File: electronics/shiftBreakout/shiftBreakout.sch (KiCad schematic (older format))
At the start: 45 parts, among them J1 Screw_Terminal_01x05, J10 Sensor C, J11 Sensor D, J2 Screw_Terminal_01x06, J3 Motor A, J4 Screw_Terminal_01x05, J5 Motor B, J6 Motor C, J7 Motor D, J8 Sensor A, J9 Sensor B, U1 74HC595, U2 TPL7407L, U3 74HC244, U4 74HC165, U5 74HC595, U6 TPL7407L, U7 74HC595, U8 TPL7407L

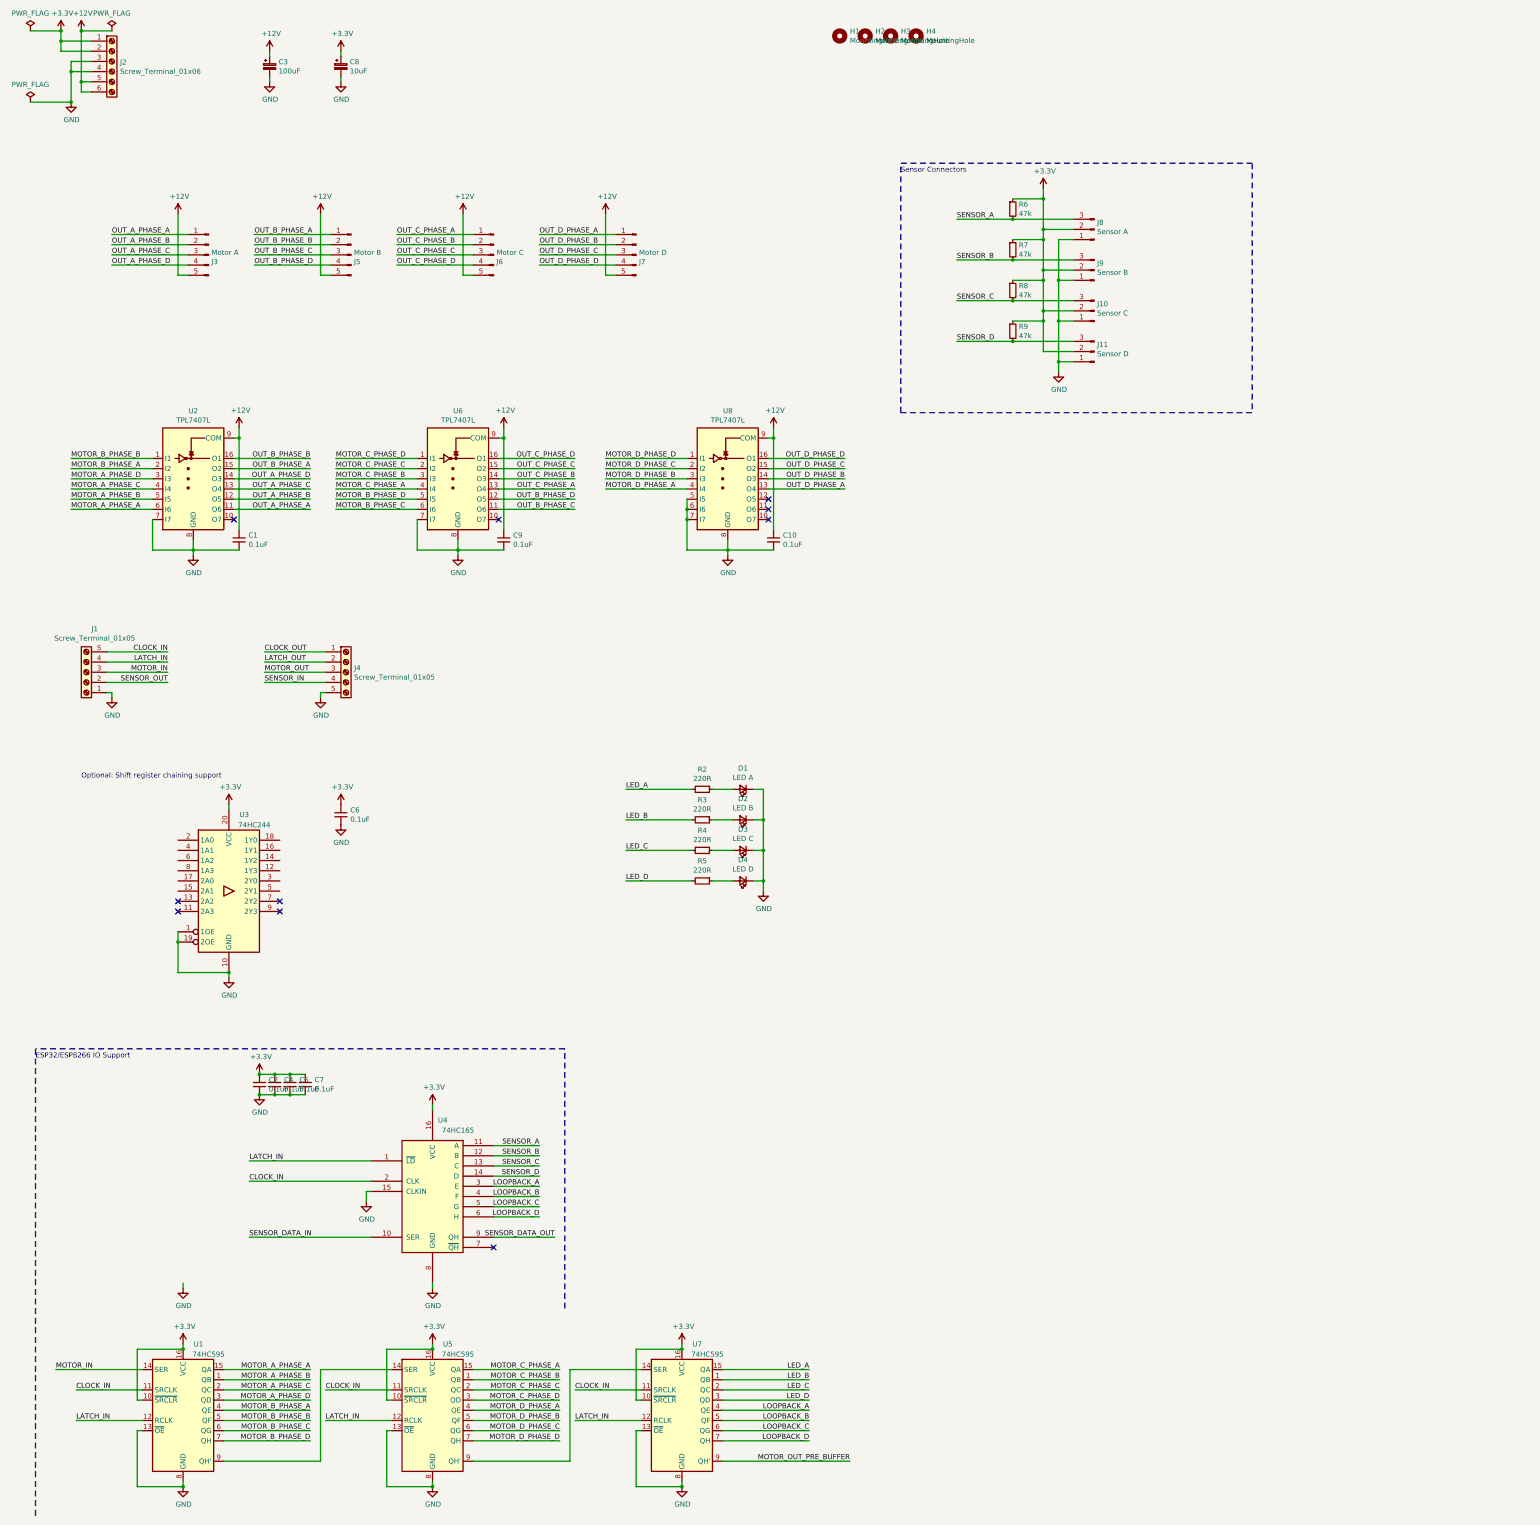
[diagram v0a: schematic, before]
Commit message: Shift breakout PCB progress
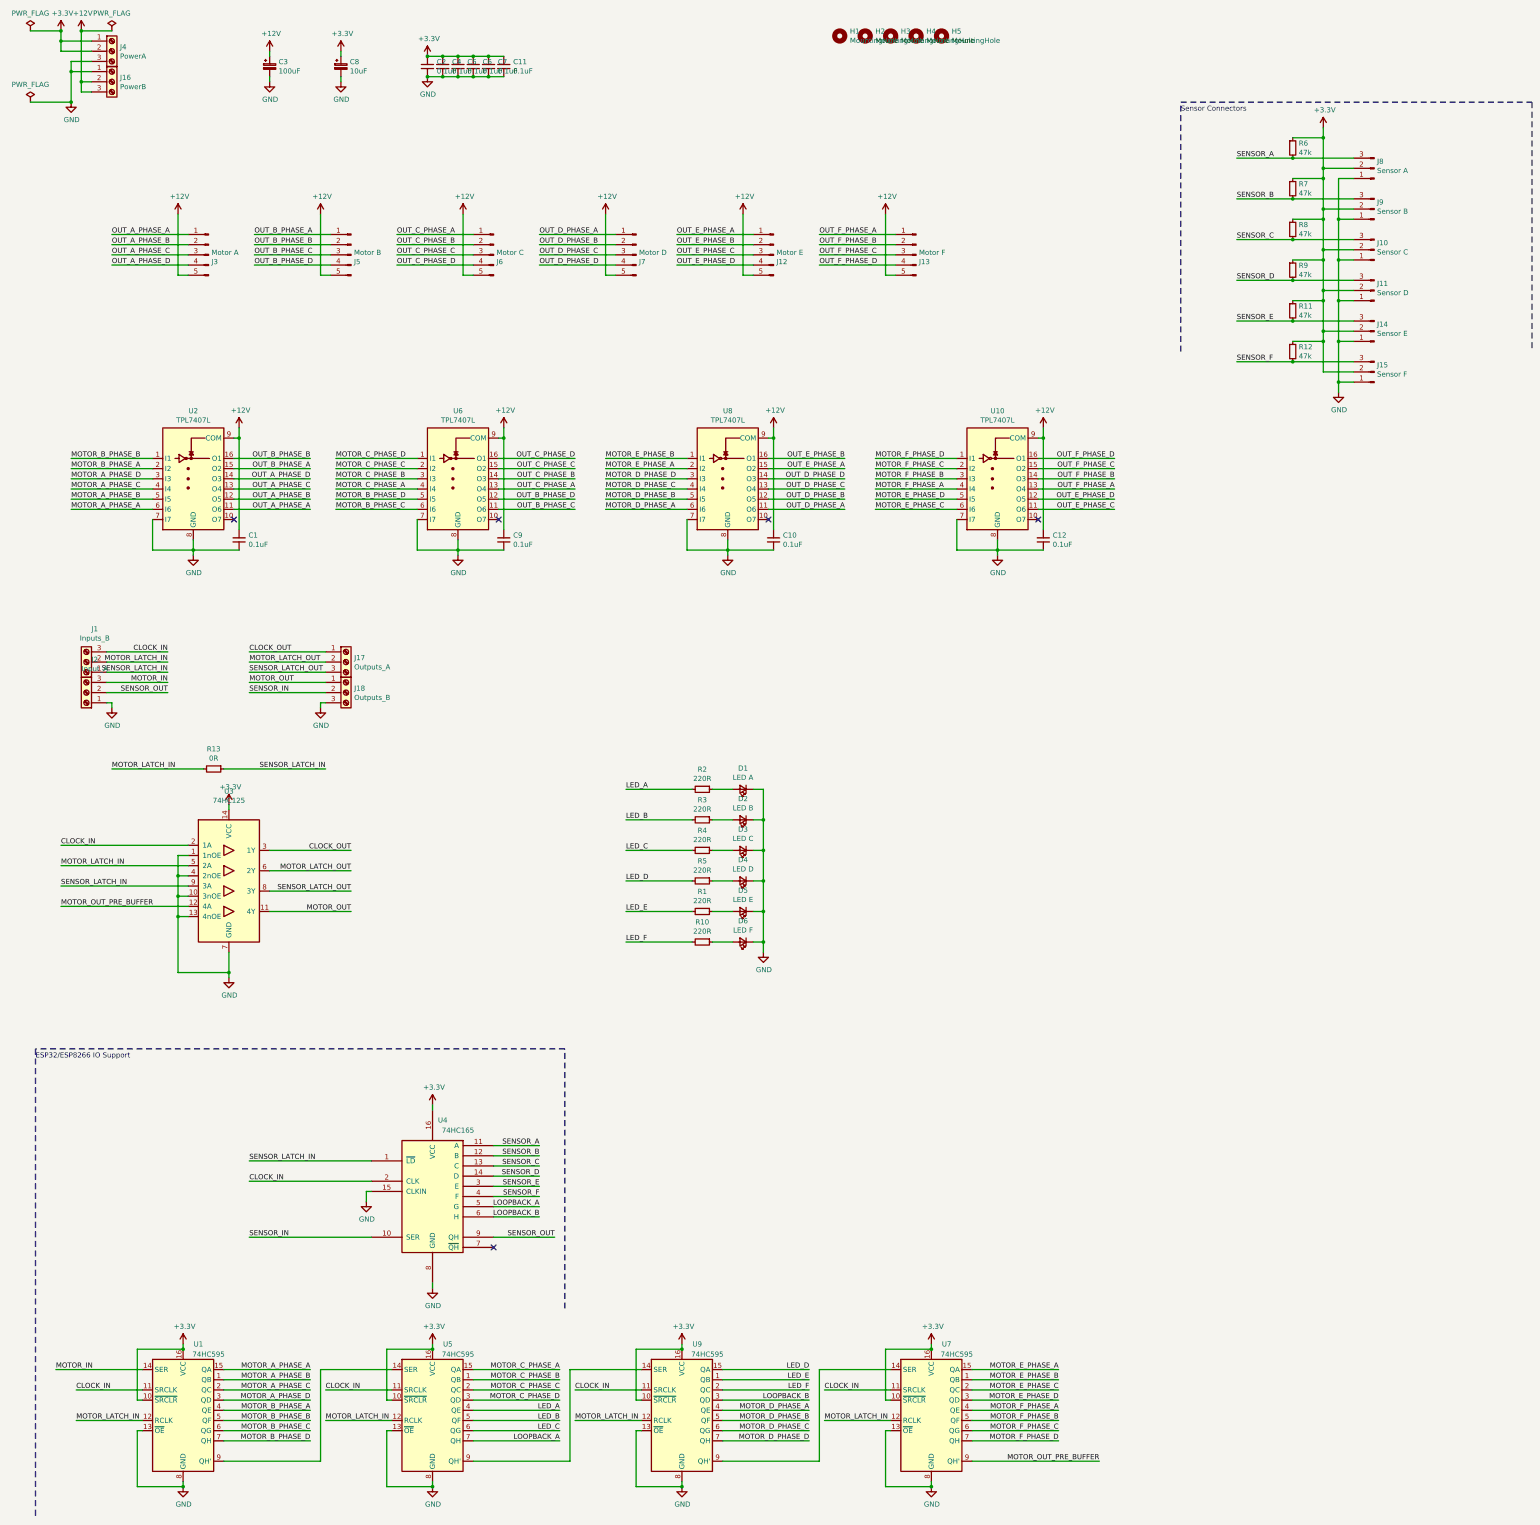
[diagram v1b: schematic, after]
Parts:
- removed J1, J4: Screw_Terminal_01x05, TerminalBlock:TerminalBlock_bornier-5_P5.08mm, symbol Connector:Screw_Terminal_01x05
- removed J2: Screw_Terminal_01x06, TerminalBlock:TerminalBlock_bornier-6_P5.08mm, symbol Connector:Screw_Terminal_01x06
- removed U3: 74HC244, Package_SO:SOIC-20W_7.5x12.8mm_P1.27mm, symbol 74xx:74HC244
- added C11, C12: 0.1uF, Capacitor_SMD:C_0603_1608Metric, symbol Device:C_Small
- added D5: LED E, ModifiedSymbols:LED_0603_1608Metric_Silkscreen, symbol Device:LED_Small
- added D6: LED F, ModifiedSymbols:LED_0603_1608Metric_Silkscreen, symbol Device:LED_Small
- added H5: MountingHole, MountingHole:MountingHole_4.3mm_M4_ISO7380_Pad, symbol Mechanical:MountingHole
- added J1: Inputs_B, TerminalBlock_Phoenix:TerminalBlock_Phoenix_MKDS-1,5-3-5.08_1x03_P5.08mm_Horizontal, symbol Connector:Screw_Terminal_01x03
- added J12: Motor E, Connector_JST:JST_XH_B5B-XH-A_1x05_P2.50mm_Vertical, symbol Connector:Conn_01x05_Male
- added J13: Motor F, Connector_JST:JST_XH_B5B-XH-A_1x05_P2.50mm_Vertical, symbol Connector:Conn_01x05_Male
- added J14: Sensor E, Connector_PinHeader_2.54mm:PinHeader_1x03_P2.54mm_Vertical, symbol Connector:Conn_01x03_Male
- added J15: Sensor F, Connector_PinHeader_2.54mm:PinHeader_1x03_P2.54mm_Vertical, symbol Connector:Conn_01x03_Male
- added J16: PowerB, TerminalBlock_Phoenix:TerminalBlock_Phoenix_MKDS-1,5-3-5.08_1x03_P5.08mm_Horizontal, symbol Connector:Screw_Terminal_01x03
- added J17: Outputs_A, TerminalBlock_Phoenix:TerminalBlock_Phoenix_MKDS-1,5-3-5.08_1x03_P5.08mm_Horizontal, symbol Connector:Screw_Terminal_01x03
- added J18: Outputs_B, TerminalBlock_Phoenix:TerminalBlock_Phoenix_MKDS-1,5-3-5.08_1x03_P5.08mm_Horizontal, symbol Connector:Screw_Terminal_01x03
- added J2: Input_A, TerminalBlock_Phoenix:TerminalBlock_Phoenix_MKDS-1,5-3-5.08_1x03_P5.08mm_Horizontal, symbol Connector:Screw_Terminal_01x03
- added J4: PowerA, TerminalBlock_Phoenix:TerminalBlock_Phoenix_MKDS-1,5-3-5.08_1x03_P5.08mm_Horizontal, symbol Connector:Screw_Terminal_01x03
- added R1, R10: 220R, Resistor_SMD:R_0603_1608Metric, symbol Device:R_Small
- added R11, R12: 47k, Resistor_SMD:R_0603_1608Metric, symbol Device:R_Small
- added R13: 0R, Resistor_SMD:R_0603_1608Metric, symbol Device:R_Small
- added U10: TPL7407L, ModifiedSymbols:SOIC-16_3.9x9.9mm_P1.27mm_silk, symbol Transistor_Array:ULN2003A
- added U3: 74HC125, ModifiedSymbols:SOIC-14_3.9x8.7mm_P1.27mm_silk, symbol 74HC125:74HC125
- added U9: 74HC595, ModifiedSymbols:SOIC-16_3.9x9.9mm_P1.27mm_silk, symbol 74xx:74HC595
- C1, C10, C2, C4, C5, C6, C7, C9: LCSC (none) -> C14663
- C3: LCSC (none) -> C176665
- C8: LCSC (none) -> C134721
- D1, D2, D3, D4: footprint LED_SMD:LED_0603_1608Metric -> ModifiedSymbols:LED_0603_1608Metric_Silkscreen; LCSC (none) -> C2286
- J3, J5, J6, J7: footprint JST_XH_Connectors:JST_XH_2-5mm_5pin -> Connector_JST:JST_XH_B5B-XH-A_1x05_P2.50mm_Vertical
- R2, R3, R4, R5: LCSC (none) -> C22962
- R6, R7, R8, R9: LCSC (none) -> C25819
- U1, U5, U7: footprint Package_SO:SOIC-16_3.9x9.9mm_P1.27mm -> ModifiedSymbols:SOIC-16_3.9x9.9mm_P1.27mm_silk; LCSC (none) -> C5947
- U2, U6, U8: footprint Package_SO:SOIC-16_3.9x9.9mm_P1.27mm -> ModifiedSymbols:SOIC-16_3.9x9.9mm_P1.27mm_silk; LCSC (none) -> C139663
- U4: footprint Package_SO:SOIC-16_3.9x9.9mm_P1.27mm -> ModifiedSymbols:SOIC-16_3.9x9.9mm_P1.27mm_silk; LCSC (none) -> C5613
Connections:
- net SENSOR_DATA_IN is gone; now on net SENSOR_IN: U4.10 (SER)
- net SENSOR_DATA_OUT is gone; now on net SENSOR_OUT: U4.9 (QH)
- net +12V: now also C12.2, J12.5 (Pin_5), J13.5 (Pin_5), J16.2 (Pin_2), J16.3 (Pin_3), U10.9 (COM)
- net +3V3: now also C11.1, J14.2 (Pin_2), J15.2 (Pin_2), J4.1 (Pin_1), J4.2 (Pin_2), R11.1, R12.1, U3.14 (VCC), U9.10 (~SRCLR), U9.16 (VCC)
- net CLOCK_IN: now also J1.3 (Pin_3), U3.2 (1A), U9.11 (SRCLK)
- net CLOCK_OUT: now also J17.1 (Pin_1), U3.3 (1Y)
- net GND: now also C11.2, C12.1, D5.1 (K), D6.1 (K), J14.1 (Pin_1), J15.1 (Pin_1), J16.1 (Pin_1), J18.3 (Pin_3), J2.1 (Pin_1), J4.3 (Pin_3), U10.7 (I7), U10.8 (GND), U3.1 (1nOE), U3.10 (3nOE), U3.13 (4nOE), U3.4 (2nOE), U3.7 (GND), U9.13 (~OE), U9.8 (GND); no longer U8.5 (I5), U8.6 (I6)
- net LED_A: now also U5.4 (QE); no longer U7.15 (QA)
- net LED_B: now also U5.5 (QF); no longer U7.1 (QB)
- net LED_C: now also U5.6 (QG); no longer U7.2 (QC)
- net LED_D: now also U9.15 (QA); no longer U7.3 (QD)
- net LOOPBACK_A: now also U4.5 (G), U5.7 (QH); no longer U4.3 (E), U7.4 (QE)
- net LOOPBACK_B: now also U4.6 (H), U9.3 (QD); no longer U4.4 (F), U7.5 (QF)
- net MOTOR_D_PHASE_A: now also U8.6 (I6), U9.4 (QE); no longer U5.4 (QE), U8.4 (I4)
- net MOTOR_D_PHASE_B: now also U8.5 (I5), U9.5 (QF); no longer U5.5 (QF), U8.3 (I3)
- net MOTOR_D_PHASE_C: now also U8.4 (I4), U9.6 (QG); no longer U5.6 (QG), U8.2 (I2)
- net MOTOR_D_PHASE_D: now also U8.3 (I3), U9.7 (QH); no longer U5.7 (QH), U8.1 (I1)
- net MOTOR_IN: now also J2.3 (Pin_3)
- net MOTOR_OUT: now also J18.1 (Pin_1), U3.11 (4Y)
- net MOTOR_OUT_PRE_BUFFER: now also U3.12 (4A)
- net OUT_D_PHASE_A: now also U8.11 (O6); no longer U8.13 (O4)
- net OUT_D_PHASE_B: now also U8.12 (O5); no longer U8.14 (O3)
- net OUT_D_PHASE_C: now also U8.13 (O4); no longer U8.15 (O2)
- net OUT_D_PHASE_D: now also U8.14 (O3); no longer U8.16 (O1)
- net SENSOR_IN: now also J18.2 (Pin_2)
- net SENSOR_OUT: now also J2.2 (Pin_2)
- net at U5.9 (QH'): now also U9.14 (SER); no longer U7.14 (SER)
- net LATCH_IN renamed MOTOR_LATCH_IN
- net MOTOR_LATCH_IN: now also J1.2 (Pin_2), R13.2, U3.5 (2A), U9.12 (RCLK); no longer U4.1 (~LD)
- net LOOPBACK_C renamed MOTOR_F_PHASE_C
- net MOTOR_F_PHASE_C: now also U10.2 (I2); no longer U4.5 (G)
- net LOOPBACK_D renamed MOTOR_F_PHASE_D
- net MOTOR_F_PHASE_D: now also U10.1 (I1); no longer U4.6 (H)
- new net: U7.14 (SER), U9.9 (QH')
- new net: D5.2 (A), R1.1
- new net: D6.2 (A), R10.1
- new net LED_E: R1.2, U9.1 (QB)
- new net LED_F: R10.2, U9.2 (QC)
- new net MOTOR_E_PHASE_A: U7.15 (QA), U8.2 (I2)
- new net MOTOR_E_PHASE_B: U7.1 (QB), U8.1 (I1)
- new net MOTOR_E_PHASE_C: U10.6 (I6), U7.2 (QC)
- new net MOTOR_E_PHASE_D: U10.5 (I5), U7.3 (QD)
- new net MOTOR_F_PHASE_A: U10.4 (I4), U7.4 (QE)
- new net MOTOR_F_PHASE_B: U10.3 (I3), U7.5 (QF)
- new net MOTOR_LATCH_OUT: J17.2 (Pin_2), U3.6 (2Y)
- new net OUT_E_PHASE_A: J12.1 (Pin_1), U8.15 (O2)
- new net OUT_E_PHASE_B: J12.2 (Pin_2), U8.16 (O1)
- new net OUT_E_PHASE_C: J12.3 (Pin_3), U10.11 (O6)
- new net OUT_E_PHASE_D: J12.4 (Pin_4), U10.12 (O5)
- new net OUT_F_PHASE_A: J13.1 (Pin_1), U10.13 (O4)
- new net OUT_F_PHASE_B: J13.2 (Pin_2), U10.14 (O3)
- new net OUT_F_PHASE_C: J13.3 (Pin_3), U10.15 (O2)
- new net OUT_F_PHASE_D: J13.4 (Pin_4), U10.16 (O1)
- new net SENSOR_E: J14.3 (Pin_3), R11.2, U4.3 (E)
- new net SENSOR_F: J15.3 (Pin_3), R12.2, U4.4 (F)
- new net SENSOR_LATCH_IN: J1.1 (Pin_1), R13.1, U3.9 (3A), U4.1 (~LD)
- new net SENSOR_LATCH_OUT: J17.3 (Pin_3), U3.8 (3Y)
- no-connect marks 10 -> 5
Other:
- note removed: "Optional: Shift register chaining support"
- moved on the sheet: C2, C4, C5, C6, C7, J10, J11, J8, J9, R6, R7, R8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

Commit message: Finished shiftBreakout PCB
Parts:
- added H6, H7: MountingHole, JLCPCB:AssemblyToolingHole, symbol Mechanical:MountingHole
- C3, C8: JLCPCB_CORRECTION (none) -> 0;0;180
- H1, H2, H3, H4, H5: footprint MountingHole:MountingHole_4.3mm_M4_ISO7380_Pad -> MountingHole:MountingHole_3.2mm_M3_ISO7380_Pad; symbol Mechanical:MountingHole -> Mechanical:MountingHole_Pad
- J1, J17, J18: footprint TerminalBlock_Phoenix:TerminalBlock_Phoenix_MKDS-1,5-3-5.08_1x03_P5.08mm_Horizontal -> ScrewTerminals:C72334_WJ500V-5.08-3P
- J16: value PowerB -> Power_B; footprint TerminalBlock_Phoenix:TerminalBlock_Phoenix_MKDS-1,5-3-5.08_1x03_P5.08mm_Horizontal -> ScrewTerminals:C72334_WJ500V-5.08-3P
- J2: value Input_A -> Inputs_A; footprint TerminalBlock_Phoenix:TerminalBlock_Phoenix_MKDS-1,5-3-5.08_1x03_P5.08mm_Horizontal -> ScrewTerminals:C72334_WJ500V-5.08-3P
- J4: value PowerA -> Power_A; footprint TerminalBlock_Phoenix:TerminalBlock_Phoenix_MKDS-1,5-3-5.08_1x03_P5.08mm_Horizontal -> ScrewTerminals:C72334_WJ500V-5.08-3P
- U1, U10, U2, U3, U4, U5, U6, U7, U8, U9: JLCPCB_CORRECTION (none) -> 0;0;-90
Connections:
- net MOTOR_IN: now also J1.2 (Pin_2); no longer J2.3 (Pin_3)
- net MOTOR_LATCH_IN: now also J2.3 (Pin_3); no longer J1.2 (Pin_2)
- net MOTOR_LATCH_OUT: now also J18.1 (Pin_1); no longer J17.2 (Pin_2)
- net MOTOR_OUT: now also J17.2 (Pin_2); no longer J18.1 (Pin_1)
- net SENSOR_IN: now also J17.3 (Pin_3); no longer J18.2 (Pin_2)
- net SENSOR_LATCH_IN: now also J2.2 (Pin_2); no longer J1.1 (Pin_1)
- net SENSOR_LATCH_OUT: now also J18.2 (Pin_2); no longer J17.3 (Pin_3)
- net SENSOR_OUT: now also J1.1 (Pin_1); no longer J2.2 (Pin_2)
- no-connect marks 5 -> 10
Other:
- note added: "Do not use O7 on TPL7407L\n(see note above)"
- note added: "JLCPCB Assembly Tooling Holes"
- note added: "Motor data does not need to be buffered for transmission reasons\n(it is 1:1 from one board to the next, not bussed), but it is buffered\nto keep timing in sync with the buffered clock.\n\n74HC595 chaining relies on narrow propagation delay > hold time\nmargin to work, so we need to be cognizant of anything that may\ncause data to change sooner after the rising clock edge (reducing\neffective pro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"
- note added: "Output and input latches can be combined using R13\nto reduce number of wires needed between boards."
- note added: "TPL7407L or TPL7407LA will work. OUT7 is avoided because the datasheet recommends an external flyback diode for TPL7407L, and we have spare channels we can use instead."
- note added: "Use shielded 5 conductor (or 4 conductor if using R13) cable.\nConnect shield to GND at both ends."
- note removed: "ESP32/ESP8266 IO Support"
- note removed: "Sensor Connectors"
- moved on the sheet: D1, D2, D3, D4, D5, D6, J10, J11, J14, J15, J16, J4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
